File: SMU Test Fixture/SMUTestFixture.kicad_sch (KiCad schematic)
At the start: 60 parts

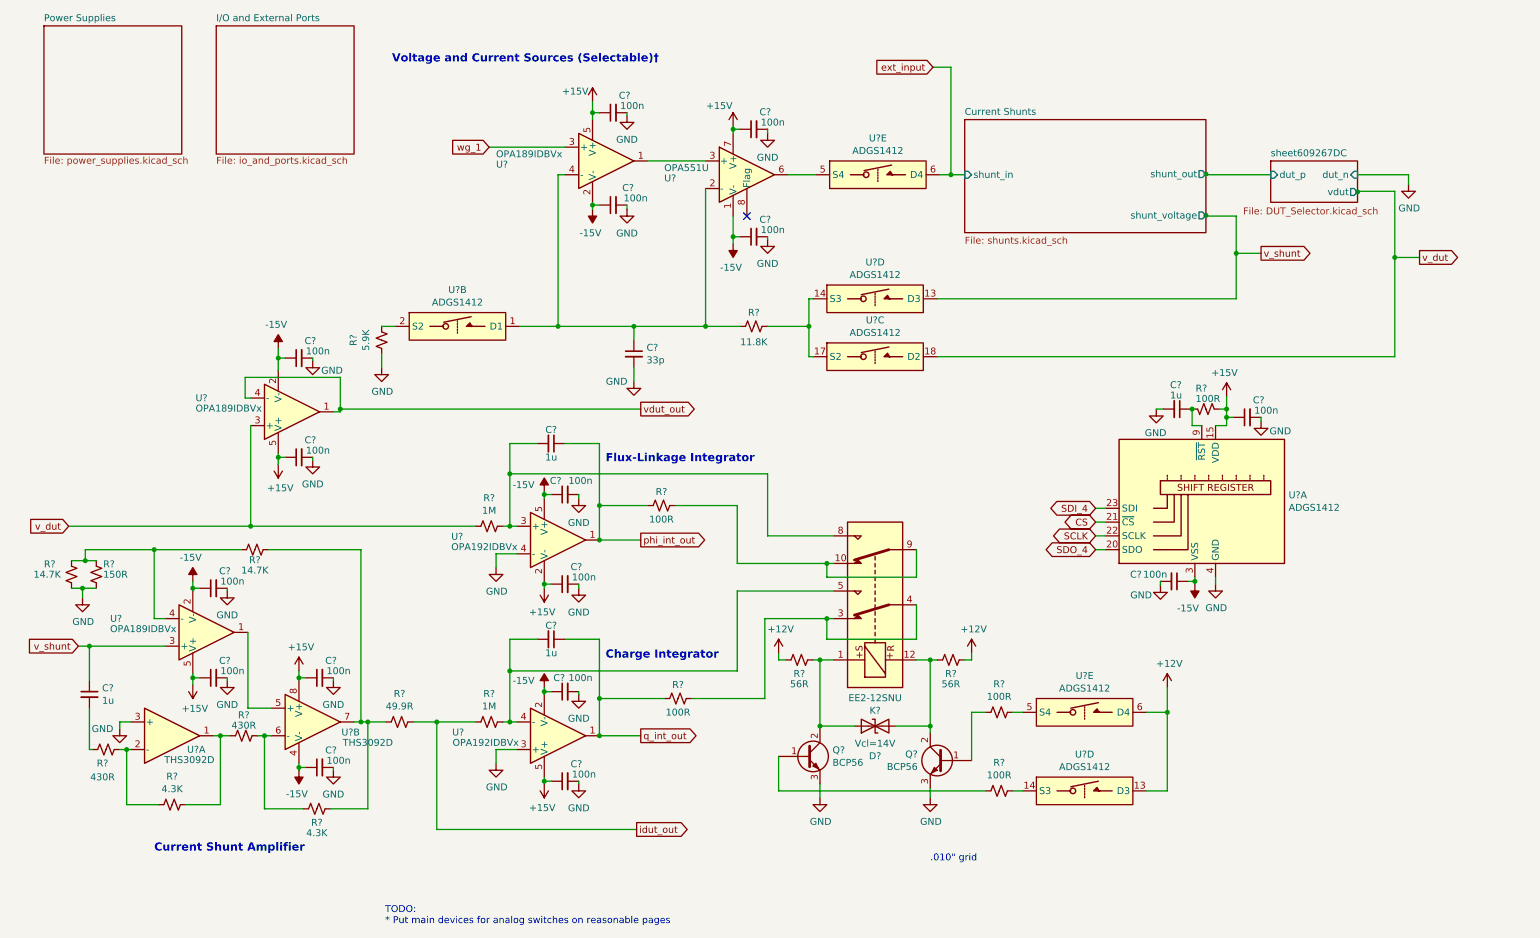
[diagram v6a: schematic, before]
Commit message: Split ADGS1408 units, add switch contorl page
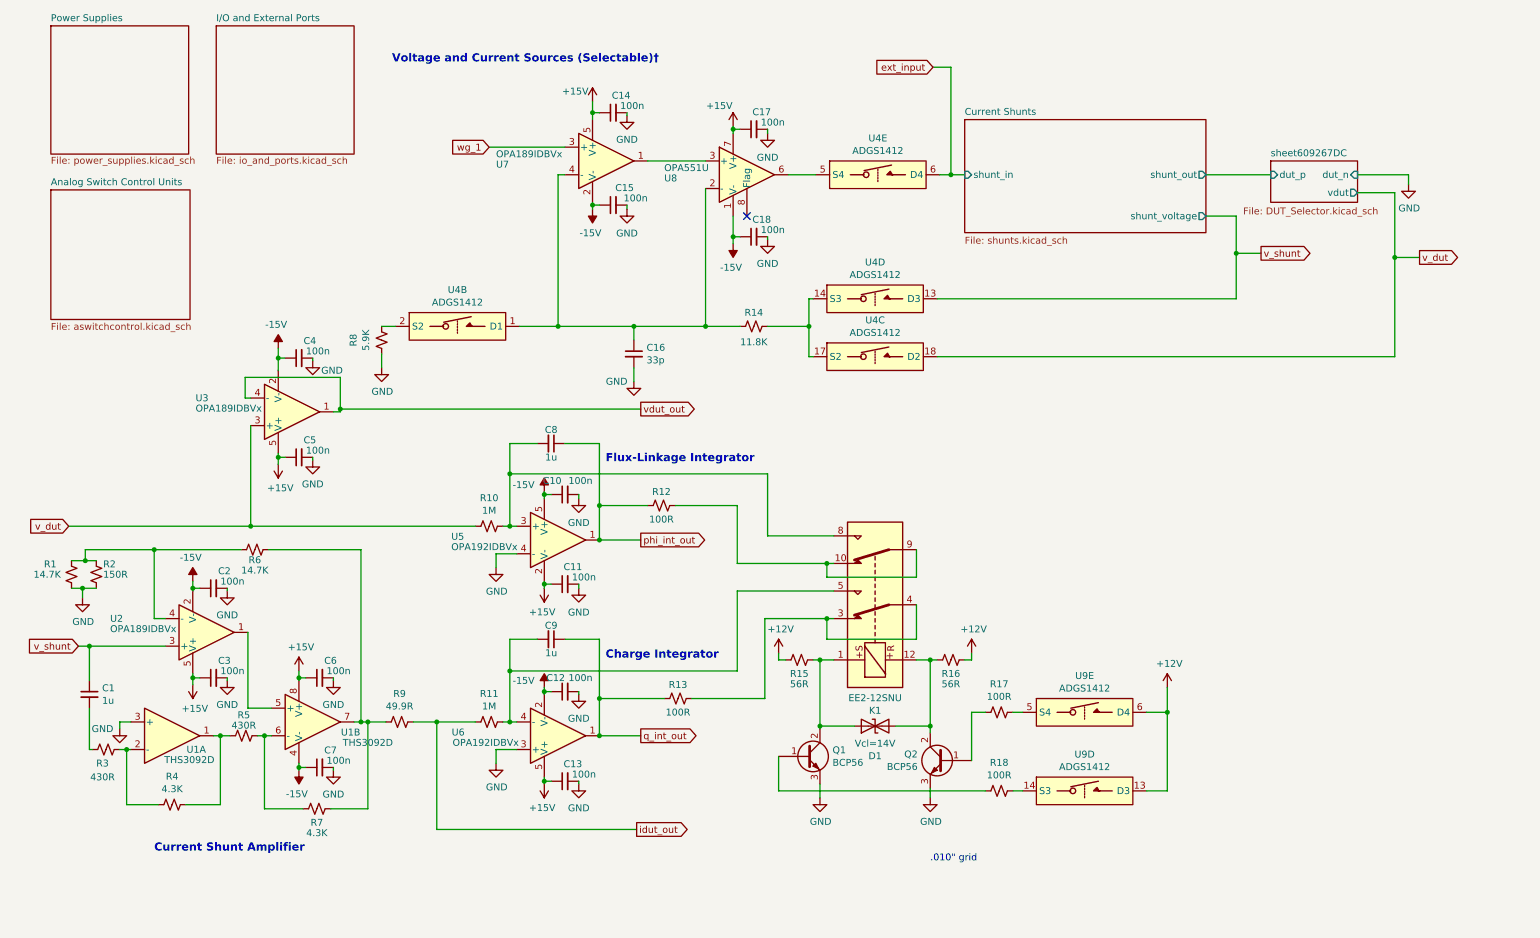
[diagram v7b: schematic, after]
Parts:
- removed C?: 1u, symbol Device:C_Small
- removed C? (x2): 100n, Capacitor_SMD:C_0805_2012Metric_Pad1.18x1.45mm_HandSolder, symbol Device:C_Small
- removed R?: 100R, symbol Device:R_Small_US
- removed U?: ADGS1412, Package_CSP:LFCSP-24-1EP_4x4mm_P0.5mm_EP2.5x2.5mm, symbol SMUTestFixture-rescue:ADGS1412-MAGI_Symbols
- gave numbers to parts that had none: 49
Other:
- added sheet Analog Switch Control Units (aswitchcontrol.kicad_sch)
- note removed: "TODO: * Put main devices for analog switches on reasonable pages"

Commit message: Symbol fixes, ERC pass
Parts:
- U7: footprint Package_TO_SOT_SMD:SOT-223-5 -> Package_TO_SOT_SMD:SOT-23-5_HandSoldering
